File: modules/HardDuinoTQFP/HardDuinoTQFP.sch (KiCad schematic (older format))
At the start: 22 parts, among them J1 Conn_01x10_Male, J2 Conn_01x10_Male, J3 Conn_01x05_Male, J4 Conn_02x03_Odd_Even, J5 Conn_01x01_Male, U1 ATmega328P-AU, Y1 16MHz

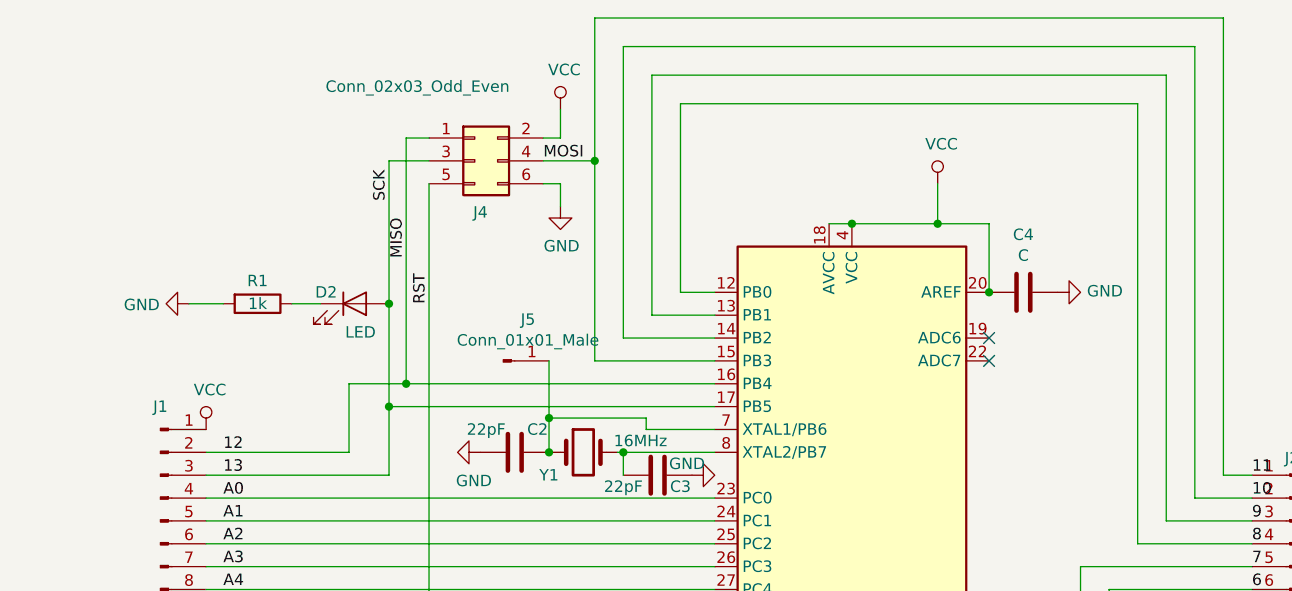
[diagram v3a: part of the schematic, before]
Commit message: HardDuinoTQFP: add protection, remove AREF
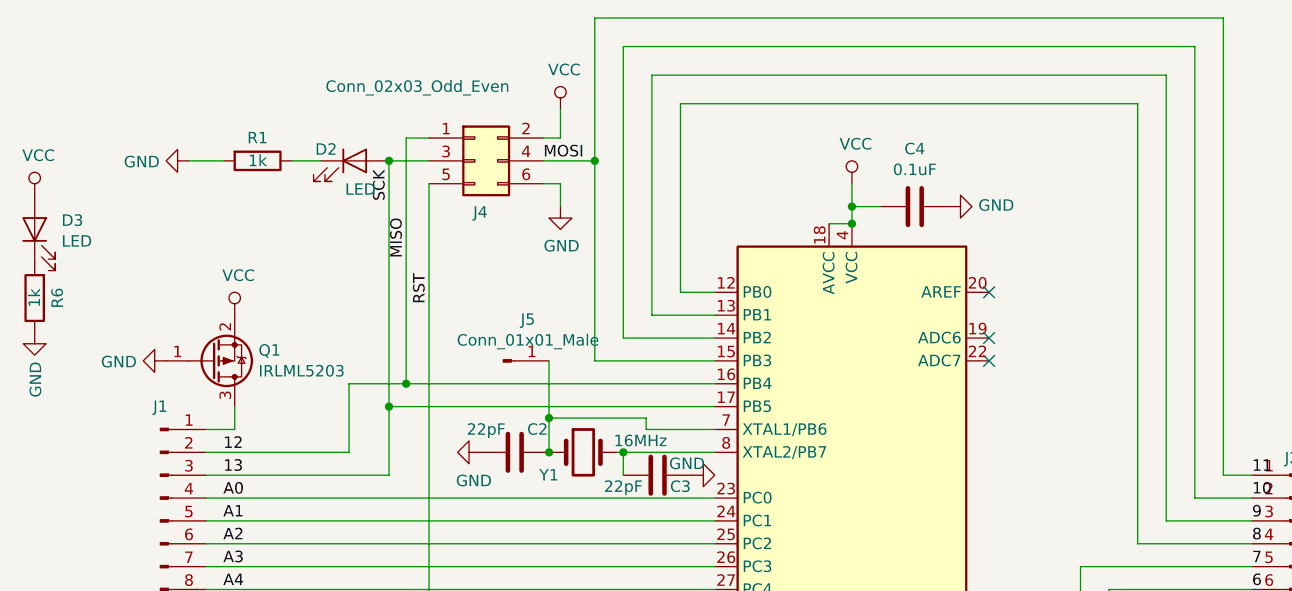
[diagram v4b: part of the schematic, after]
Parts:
- added D3: LED, LED_SMD:LED_0805_2012Metric_Pad1.15x1.40mm_HandSolder, symbol Device:LED
- added Q1: IRLML5203, Package_TO_SOT_SMD:SOT-23, symbol Transistor_FET:IRLML5203
- added R6: 1k, Resistor_SMD:R_0805_2012Metric_Pad1.15x1.40mm_HandSolder, symbol Device:R
- C4: value C -> 0.1uF
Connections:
- net GND: now also Q1.1 (G), R6.1
- net VCC: now also D3.2 (A), Q1.2 (S); no longer J1.1 (Pin_1), U1.20 (AREF)
- new net: J1.1 (Pin_1), Q1.3 (D)
- new net: D3.1 (K), R6.2
- no-connect marks 2 -> 3
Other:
- moved on the sheet: C4, D2, R1
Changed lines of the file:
@@
 L power:VCC #PWR01001
 U 1 1 5E7CBCBE
-P 2175 2550
-F 0 "#PWR01001" H 2175 2400 50  0001 C CNN
-F 1 "VCC" H 2192 2723 50  0000 C CNN
-F 2 "" H 2175 2550 50  0001 C CNN
-F 3 "" H 2175 2550 50  0001 C CNN
-	1    2175 2550
+P 2300 2050
+F 0 "#PWR01001" H 2300 1900 50  0001 C CNN
+F 1 "VCC" H 2317 2223 50  0000 C CNN
+F 2 "" H 2300 2050 50  0001 C CNN
+F 3 "" H 2300 2050 50  0001 C CNN
+	1    2300 2050
 	1    0    0    -1
 $EndComp
@@
 L Device:LED D2
 U 1 1 5EC11726
-P 2825 2000
-F 0 "D2" H 2700 2050 50  0000 C CNN
-F 1 "LED" H 2850 1875 50  0000 C CNN
-F 2 "LED_SMD:LED_0805_2012Metric_Pad1.15x1.40mm_HandSolder" H 2825 2000 50  0001 C CNN
-F 3 "~" H 2825 2000 50  0001 C CNN
-	1    2825 2000
+P 2825 1375
+F 0 "D2" H 2700 1425 50  0000 C CNN
+F 1 "LED" H 2850 1250 50  0000 C CNN
+F 2 "LED_SMD:LED_0805_2012Metric_Pad1.15x1.40mm_HandSolder" H 2825 1375 50  0001 C CNN
+F 3 "~" H 2825 1375 50  0001 C CNN
+	1    2825 1375
 	1    0    0    -1
 $EndComp
@@
 L Device:R R1
 U 1 1 5EC11FBF
-P 2400 2000
-F 0 "R1" V 2300 2000 50  0000 C CNN
-F 1 "1k" V 2400 2000 50  0000 C CNN
-F 2 "Resistor_SMD:R_0805_2012Metric_Pad1.15x1.40mm_HandSolder" V 2330 2000 50  0001 C CNN
-F 3 "~" H 2400 2000 50  0001 C CNN
-	1    2400 2000
+P 2400 1375
+F 0 "R1" V 2300 1375 50  0000 C CNN
+F 1 "1k" V 2400 1375 50  0000 C CNN
+F 2 "Resistor_SMD:R_0805_2012Metric_Pad1.15x1.40mm_HandSolder" V 2330 1375 50  0001 C CNN
+F 3 "~" H 2400 1375 50  0001 C CNN
+	1    2400 1375
 	0    1    1    0
 $EndComp
@@
 L power:GND #PWR02
 U 1 1 5EC15A85
-P 2100 2000
-F 0 "#PWR02" H 2100 1750 50  0001 C CNN
-F 1 "GND" V 2105 1872 50  0000 R CNN
-F 2 "" H 2100 2000 50  0001 C CNN
-F 3 "" H 2100 2000 50  0001 C CNN
-	1    2100 2000
-	0    1    1    0
-$EndComp
-Wire Wire Line
-	2100 2000 2250 2000
-Wire Wire Line
-	2550 2000 2675 2000
+P 2100 1375
+F 0 "#PWR02" H 2100 1125 50  0001 C CNN
+F 1 "GND" V 2105 1247 50  0000 R CNN
+F 2 "" H 2100 1375 50  0001 C CNN
+F 3 "" H 2100 1375 50  0001 C CNN
+	1    2100 1375
+	0    1    1    0
+$EndComp
+Wire Wire Line
+	2100 1375 2250 1375
+Wire Wire Line
+	2550 1375 2675 1375
 $Comp
 L Device:Crystal Y1
@@
 L power:VCC #PWR010
 U 1 1 5EC4CC66
-P 5375 1475
-F 0 "#PWR010" H 5375 1325 50  0001 C CNN
-F 1 "VCC" H 5392 1648 50  0000 C CNN
-F 2 "" H 5375 1475 50  0001 C CNN
-F 3 "" H 5375 1475 50  0001 C CNN
-	1    5375 1475
+P 5000 1475
+F 0 "#PWR010" H 5000 1325 50  0001 C CNN
+F 1 "VCC" H 5017 1648 50  0000 C CNN
+F 2 "" H 5000 1475 50  0001 C CNN
+F 3 "" H 5000 1475 50  0001 C CNN
+	1    5000 1475
 	1    0    0    -1
 $EndComp
 Wire Wire Line
 	4900 1650 5000 1650
-Wire Wire Line
-	5000 1650 5375 1650
-Wire Wire Line
-	5600 1650 5600 1950
-Connection ~ 5000 1650
-Wire Wire Line
-	5375 1475 5375 1650
-Connection ~ 5375 1650
-Wire Wire Line
-	5375 1650 5600 1650
 $Comp
 L power:GND #PWR09
@@
 L Device:C C4
 U 1 1 5EC58145
-P 5750 1950
-F 0 "C4" V 5498 1950 50  0000 C CNN
-F 1 "C" V 5589 1950 50  0000 C CNN
-F 2 "Capacitor_SMD:C_0805_2012Metric_Pad1.15x1.40mm_HandSolder" H 5788 1800 50  0001 C CNN
-F 3 "~" H 5750 1950 50  0001 C CNN
-	1    5750 1950
-	0    1    1    0
-$EndComp
-Connection ~ 5600 1950
+P 5275 1575
+F 0 "C4" V 5023 1575 50  0000 C CNN
+F 1 "0.1uF" V 5114 1575 50  0000 C CNN
+F 2 "Capacitor_SMD:C_0805_2012Metric_Pad1.15x1.40mm_HandSolder" H 5313 1425 50  0001 C CNN
+F 3 "~" H 5275 1575 50  0001 C CNN
+	1    5275 1575
+	0    1    1    0
+$EndComp
 $Comp
 L power:GND #PWR011
 U 1 1 5EC5BFE8
-P 5900 1950
-F 0 "#PWR011" H 5900 1700 50  0001 C CNN
-F 1 "GND" V 5905 1822 50  0000 R CNN
-F 2 "" H 5900 1950 50  0001 C CNN
-F 3 "" H 5900 1950 50  0001 C CNN
-	1    5900 1950
+P 5425 1575
+F 0 "#PWR011" H 5425 1325 50  0001 C CNN
+F 1 "GND" V 5430 1447 50  0000 R CNN
+F 2 "" H 5425 1575 50  0001 C CNN
+F 3 "" H 5425 1575 50  0001 C CNN
+	1    5425 1575
 	0    -1   -1   0
 $EndComp
@@
 Wire Wire Line
 	2800 2350 3050 2350
-Wire Wire Line
-	2975 2000 2975 2450
 Wire Wire Line
 	2975 2450 4400 2450
@@
 	3875 1375 3875 2250
 Wire Wire Line
-	2975 2000 2975 1375
-Wire Wire Line
 	2975 1375 3150 1375
-Connection ~ 2975 2000
 Wire Wire Line
 	3050 1275 3050 2350
@@
 	3675 2250 3675 2500
 Connection ~ 3675 2500
+Wire Wire Line
+	5000 1650 5000 1575
+Connection ~ 5000 1650
+Wire Wire Line
+	5125 1575 5000 1575
+Connection ~ 5000 1575
+Wire Wire Line
+	5000 1575 5000 1475
+NoConn ~ 5600 1950
+$Comp
+L Transistor_FET:IRLML5203 Q1
+U 1 1 5ED6E3DF
+P 2200 2250
+F 0 "Q1" H 2404 2204 50  0000 L CNN
+F 1 "IRLML5203" H 2404 2295 50  0000 L CNN
+F 2 "Package_TO_SOT_SMD:SOT-23" H 2400 2175 50  0001 L CIN
+F 3 "https://www.infineon.com/dgdl/irlml5203pbf.pdf?fileId=5546d462533600a40153566868da261d" H 2200 2250 50  0001 L CNN
+	1    2200 2250
+	1    0    0    1
+$EndComp
+Connection ~ 2975 1375
+Wire Wire Line
+	2975 1375 2975 2450
+Wire Wire Line
+	2175 2550 2300 2550
+Wire Wire Line
+	2300 2550 2300 2450
+$Comp
+L power:GND #PWR0103
+U 1 1 5ED7FEB8
+P 2000 2250
+F 0 "#PWR0103" H 2000 2000 50  0001 C CNN
+F 1 "GND" V 2005 2122 50  0000 R CNN
+F 2 "" H 2000 2250 50  0001 C CNN
+F 3 "" H 2000 2250 50  0001 C CNN
+	1    2000 2250
+	0    1    1    0
+$EndComp
+$Comp
+L Device:LED D3
+U 1 1 5ED8654A
+P 1425 1675
+F 0 "D3" V 1464 1558 50  0000 R CNN
+F 1 "LED" V 1373 1558 50  0000 R CNN
+F 2 "LED_SMD:LED_0805_2012Metric_Pad1.15x1.40mm_HandSolder" H 1425 1675 50  0001 C CNN
+F 3 "~" H 1425 1675 50  0001 C CNN
+	1    1425 1675
+	0    -1   -1   0
+$EndComp
+$Comp
+L Device:R R6
+U 1 1 5ED937CF
+P 1425 1975
+F 0 "R6" V 1325 1975 50  0000 C CNN
+F 1 "1k" V 1425 1975 50  0000 C CNN
+F 2 "Resistor_SMD:R_0805_2012Metric_Pad1.15x1.40mm_HandSolder" V 1355 1975 50  0001 C CNN
+F 3 "~" H 1425 1975 50  0001 C CNN
+	1    1425 1975
+	-1   0    0    1
+$EndComp
+$Comp
+L power:GND #PWR015
+U 1 1 5ED98336
+P 1425 2125
+F 0 "#PWR015" H 1425 1875 50  0001 C CNN
+F 1 "GND" V 1430 1997 50  0000 R CNN
+F 2 "" H 1425 2125 50  0001 C CNN
+F 3 "" H 1425 2125 50  0001 C CNN
+	1    1425 2125
+	1    0    0    -1
+$EndComp
+$Comp
+L power:VCC #PWR014
+U 1 1 5EDA4D5C
+P 1425 1525
+F 0 "#PWR014" H 1425 1375 50  0001 C CNN
+F 1 "VCC" H 1442 1698 50  0000 C CNN
+F 2 "" H 1425 1525 50  0001 C CNN
+F 3 "" H 1425 1525 50  0001 C CNN
+	1    1425 1525
+	1    0    0    -1
+$EndComp
 $EndSCHEMATC

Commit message: HardDuinoTQFP polishing
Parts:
- added R7: 1k, Resistor_SMD:R_0805_2012Metric_Pad1.15x1.40mm_HandSolder, symbol Device:R
- added R8: 1M, Resistor_SMD:R_0805_2012Metric_Pad1.15x1.40mm_HandSolder, symbol Device:R
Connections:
- net VCC: now also R7.1
- net at U1.20 (AREF): now also R7.2
- net at C2.1, J5.1 (Pin_1), U1.7 (XTAL1/PB6)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: now also R8.1
- net at C3.2, U1.8 (XTAL2/PB7), Y1.2: now also R8.2
- no-connect marks 3 -> 2
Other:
- note added: "Blink"
- note added: "ISP"
- note added: "Power"
- note added: "Power In"
- note added: "Reset"
- note added: "Reverse\npolarity\nprotection"
- note added: "To CH340/etc"
- moved on the sheet: C2, C3, D2, D3, R1, R6, Y1
